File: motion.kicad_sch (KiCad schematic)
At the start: 6 parts, among them U5 LIS3DH

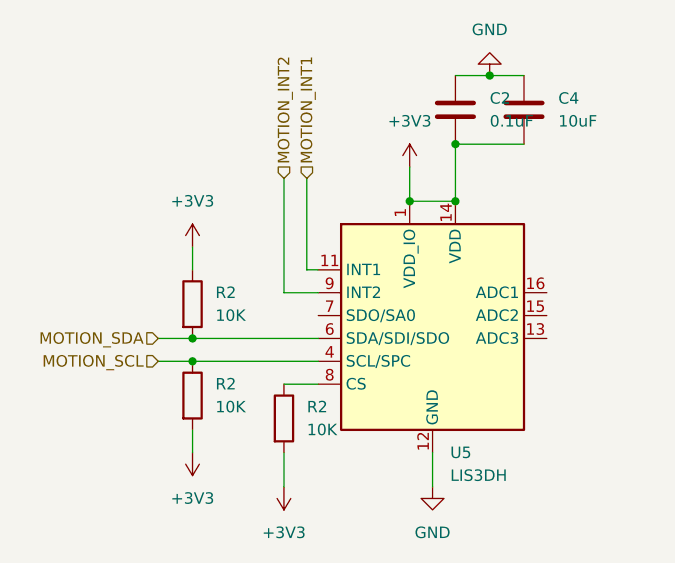
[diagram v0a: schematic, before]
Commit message: Removed audio, more routing
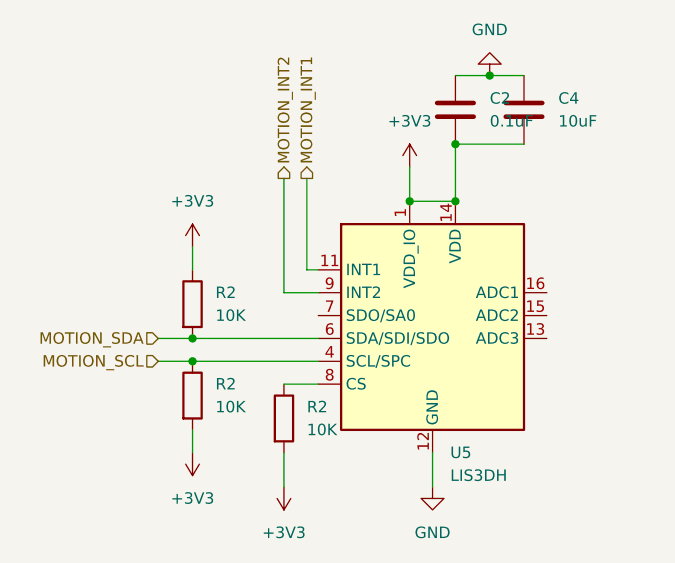
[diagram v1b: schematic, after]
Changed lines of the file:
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@@
     (stroke (width 0) (type default))
   )
-  (hierarchical_label "MOTION_INT1" (shape input) (at 109.22 68.58 90) (fields_autoplaced)
+  (hierarchical_label "MOTION_INT1" (shape output) (at 109.22 68.58 90) (fields_autoplaced)
     (effects (font (size 1.27 1.27)) (justify left))
   )
@@
     (effects (font (size 1.27 1.27)) (justify right))
   )
-  (hierarchical_label "MOTION_INT2" (shape input) (at 106.68 68.58 90) (fields_autoplaced)
+  (hierarchical_label "MOTION_INT2" (shape output) (at 106.68 68.58 90) (fields_autoplaced)
     (effects (font (size 1.27 1.27)) (justify left))
   )

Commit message: Field updates, generating fab files
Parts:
- C2: value 0.1uF -> 0.1uF 20%; JLCPCB Part # (none) -> C359190
- C4: value 10uF -> 10uF 20%; JLCPCB Part # (none) -> C315248
- R2: value 10K -> 10K 5%; JLCPCB Part # (none) -> C2906885
- U5: value LIS3DH -> LIS3DHTR; JLCPCB Part # (none) -> C15134
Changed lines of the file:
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@@
       (effects (font (size 1.27 1.27)) (justify left))
     )
-    (property "Value" "10K" (at 109.22 96.52 0)
+    (property "Value" "10K 5%" (at 109.22 96.52 0)
       (effects (font (size 1.27 1.27)) (justify left))
     )
@@
       (effects (font (size 1.27 1.27)) hide)
     )
-    (property "Datasheet" "~" (at 106.68 95.25 0)
+    (property "Datasheet" "https://www.lcsc.com/product-detail/Chip-Resistor-Surface-Mount_FOJAN-FRC0402J103-TS_C2906885.html" (at 106.68 95.25 0)
+      (effects (font (size 1.27 1.27)) hide)
+    )
+    (property "JLCPCB Part #" "C2906885" (at 106.68 95.25 0)
       (effects (font (size 1.27 1.27)) hide)
     )
@@
       (effects (font (size 1.27 1.27)) (justify left))
     )
-    (property "Value" "LIS3DH" (at 125.1459 101.6 0)
+    (property "Value" "LIS3DHTR" (at 125.1459 101.6 0)
       (effects (font (size 1.27 1.27)) (justify left))
     )
@@
     )
     (property "Datasheet" "https://www.st.com/resource/en/datasheet/cd00274221.pdf" (at 118.11 86.36 0)
+      (effects (font (size 1.27 1.27)) hide)
+    )
+    (property "JLCPCB Part #" "C15134" (at 123.19 83.82 0)
       (effects (font (size 1.27 1.27)) hide)
     )
@@
       (effects (font (size 1.27 1.27)) (justify left))
     )
-    (property "Value" "10uF" (at 137.16 62.23 0)
+    (property "Value" "10uF 20%" (at 137.16 62.23 0)
       (effects (font (size 1.27 1.27)) (justify left))
     )
@@
       (effects (font (size 1.27 1.27)) hide)
     )
-    (property "Datasheet" "~" (at 133.35 60.96 0)
+    (property "Datasheet" "https://www.lcsc.com/product-detail/Multilayer-Ceramic-Capacitors-MLCC-SMD-SMT_Samsung-Electro-Mechanics-CL05A106MP5NUNC_C315248.html" (at 133.35 60.96 0)
+      (effects (font (size 1.27 1.27)) hide)
+    )
+    (property "JLCPCB Part #" "C315248" (at 133.35 60.96 0)
       (effects (font (size 1.27 1.27)) hide)
     )
@@
       (effects (font (size 1.27 1.27)) (justify left))
     )
-    (property "Value" "10K" (at 99.06 83.82 0)
+    (property "Value" "10K 5%" (at 99.06 83.82 0)
       (effects (font (size 1.27 1.27)) (justify left))
     )
@@
       (effects (font (size 1.27 1.27)) hide)
     )
-    (property "Datasheet" "~" (at 96.52 82.55 0)
+    (property "Datasheet" "https://www.lcsc.com/product-detail/Chip-Resistor-Surface-Mount_FOJAN-FRC0402J103-TS_C2906885.html" (at 96.52 82.55 0)
+      (effects (font (size 1.27 1.27)) hide)
+    )
+    (property "JLCPCB Part #" "C2906885" (at 96.52 82.55 0)
       (effects (font (size 1.27 1.27)) hide)
     )
@@
       (effects (font (size 1.27 1.27)) (justify left))
     )
-    (property "Value" "10K" (at 99.06 93.98 0)
+    (property "Value" "10K 5%" (at 99.06 93.98 0)
       (effects (font (size 1.27 1.27)) (justify left))
     )
@@
       (effects (font (size 1.27 1.27)) hide)
     )
-    (property "Datasheet" "~" (at 96.52 92.71 0)
+    (property "Datasheet" "https://www.lcsc.com/product-detail/Chip-Resistor-Surface-Mount_FOJAN-FRC0402J103-TS_C2906885.html" (at 96.52 92.71 0)
+      (effects (font (size 1.27 1.27)) hide)
+    )
+    (property "JLCPCB Part #" "C2906885" (at 96.52 92.71 0)
       (effects (font (size 1.27 1.27)) hide)
     )
@@
       (effects (font (size 1.27 1.27)) (justify left))
     )
-    (property "Value" "0.1uF" (at 129.54 62.23 0)
+    (property "Value" "0.1uF 20%" (at 129.54 62.23 0)
       (effects (font (size 1.27 1.27)) (justify left))
     )
@@
       (effects (font (size 1.27 1.27)) hide)
     )
-    (property "Datasheet" "~" (at 125.73 60.96 0)
-      (effects (font (size 1.27 1.27)) hide)
-    )
+    (property "Datasheet" "https://www.lcsc.com/product-detail/Multilayer-Ceramic-Capacitors-MLCC-SMD-SMT_CCTC-TCC0402X5R104M250AT_C359190.html" (at 125.73 60.96 0)
+      (effects (font (size 1.27 1.27)) hide)
+    )
+    (property "JLCPCB Part #" "C359190" (at 125.73 60.96 0)
+      (effects (font (size 1.27 1.27)) hide)
+    )

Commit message: Changed outline for DFM
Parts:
- C2: JLCPCB Part # C359190 -> (none); LCSC (none) -> C359190
- C4: JLCPCB Part # C315248 -> (none); LCSC (none) -> C315248
- R2: JLCPCB Part # C2906885 -> (none); LCSC (none) -> C2906885
- U5: JLCPCB Part # C15134 -> (none); LCSC (none) -> C15134
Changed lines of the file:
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@@
       (effects (font (size 1.27 1.27)) hide)
     )
-    (property "JLCPCB Part #" "C2906885" (at 106.68 95.25 0)
+    (property "LCSC" "C2906885" (at 106.68 95.25 0)
       (effects (font (size 1.27 1.27)) hide)
     )
@@
       (effects (font (size 1.27 1.27)) hide)
     )
-    (property "JLCPCB Part #" "C15134" (at 123.19 83.82 0)
+    (property "LCSC" "C15134" (at 123.19 83.82 0)
       (effects (font (size 1.27 1.27)) hide)
     )
@@
       (effects (font (size 1.27 1.27)) hide)
     )
-    (property "JLCPCB Part #" "C315248" (at 133.35 60.96 0)
+    (property "LCSC" "C315248" (at 133.35 60.96 0)
       (effects (font (size 1.27 1.27)) hide)
     )
@@
       (effects (font (size 1.27 1.27)) hide)
     )
-    (property "JLCPCB Part #" "C2906885" (at 96.52 82.55 0)
+    (property "LCSC" "C2906885" (at 96.52 82.55 0)
       (effects (font (size 1.27 1.27)) hide)
     )
@@
       (effects (font (size 1.27 1.27)) hide)
     )
-    (property "JLCPCB Part #" "C2906885" (at 96.52 92.71 0)
+    (property "LCSC" "C2906885" (at 96.52 92.71 0)
       (effects (font (size 1.27 1.27)) hide)
     )
@@
       (effects (font (size 1.27 1.27)) hide)
     )
-    (property "JLCPCB Part #" "C359190" (at 125.73 60.96 0)
-      (effects (font (size 1.27 1.27)) hide)
-    )
+    (property "LCSC" "C359190" (at 125.73 60.96 0)
+      (effects (font (size 1.27 1.27)) hide)
+    )
